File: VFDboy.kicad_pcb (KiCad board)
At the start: 2 copper layers, 139.5 x 60 mm, 120 parts, among them J1 AVR-ISP-6, J2 USB_C_Receptacle_USB2.0, J3 Micro_SD_Card_Det, J4 TagConnect_TC2030_SWD, Q1 FS8205A, Q2 S9015, Q3 AO3401A, Q4 AO3401A, Q5 S9015, Q6 2N7002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

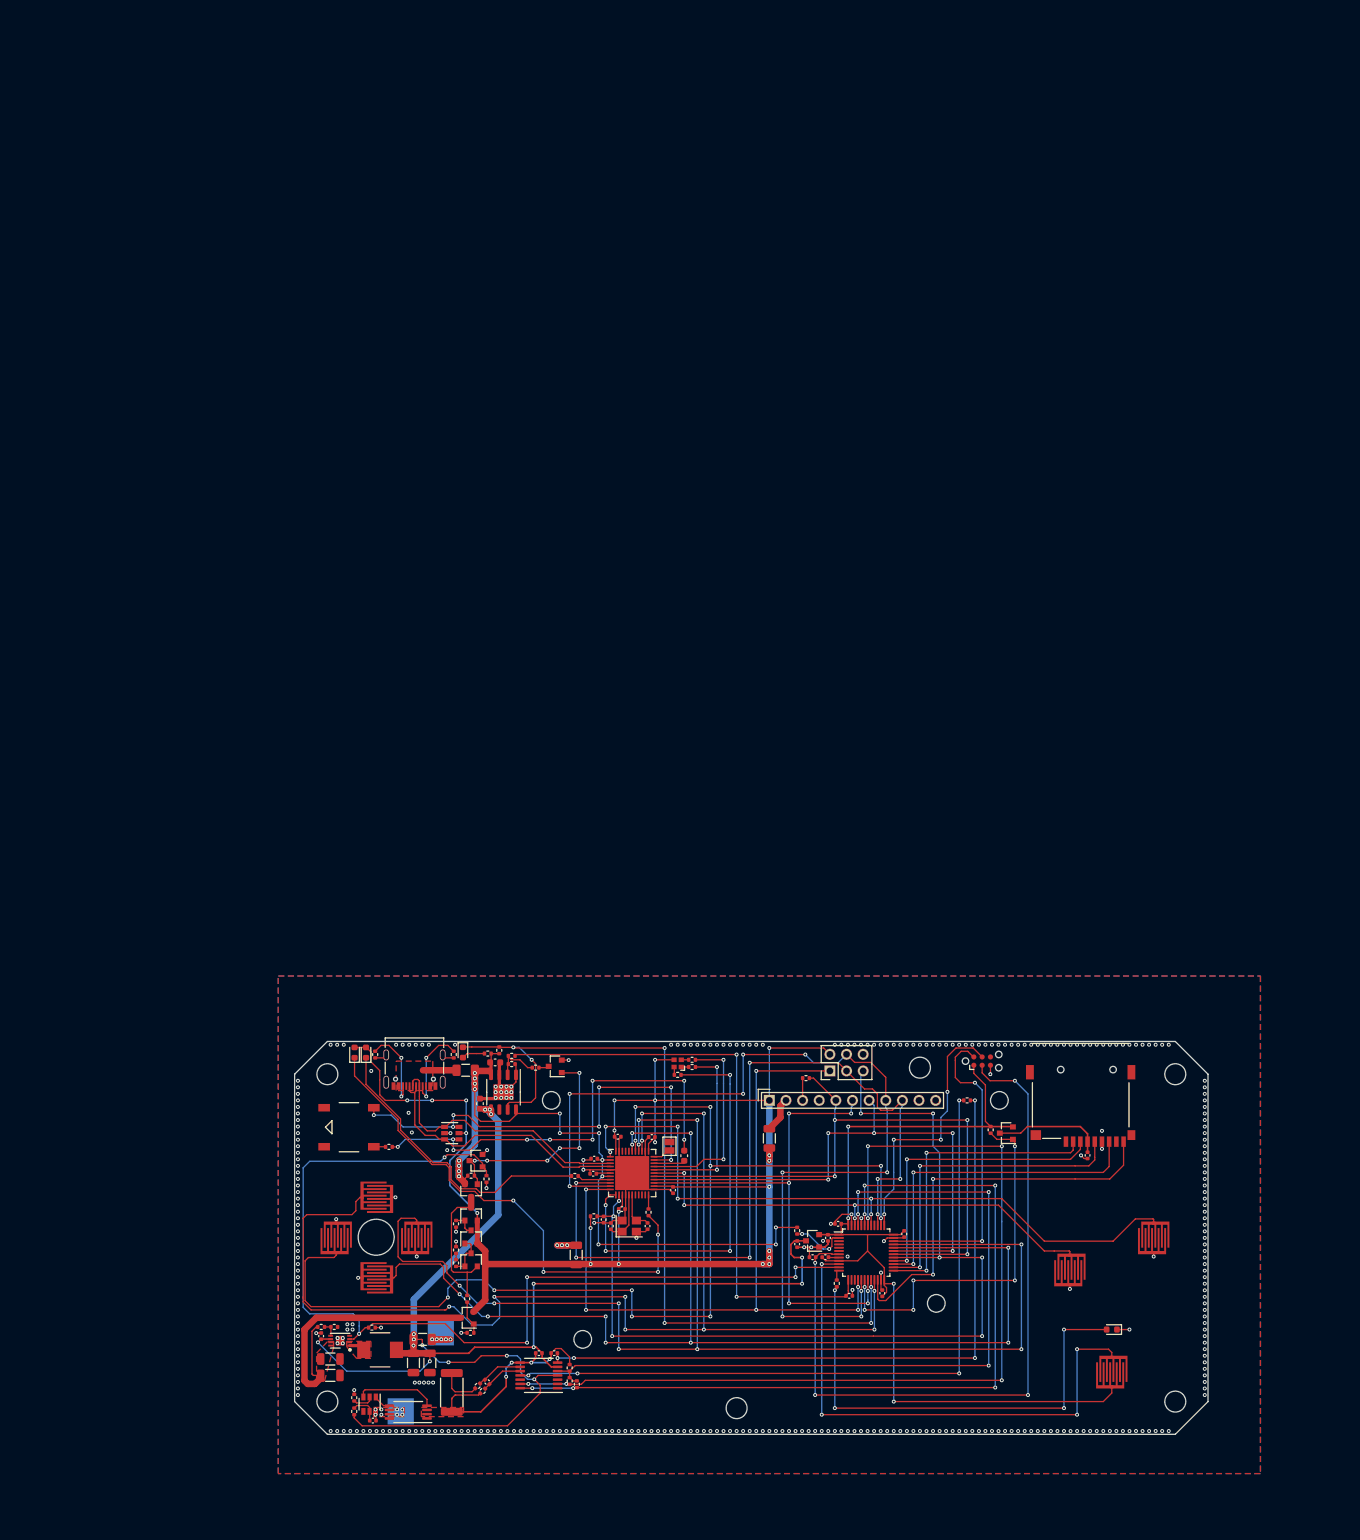
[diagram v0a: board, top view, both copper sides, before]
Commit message: Replace test points by battery footprints
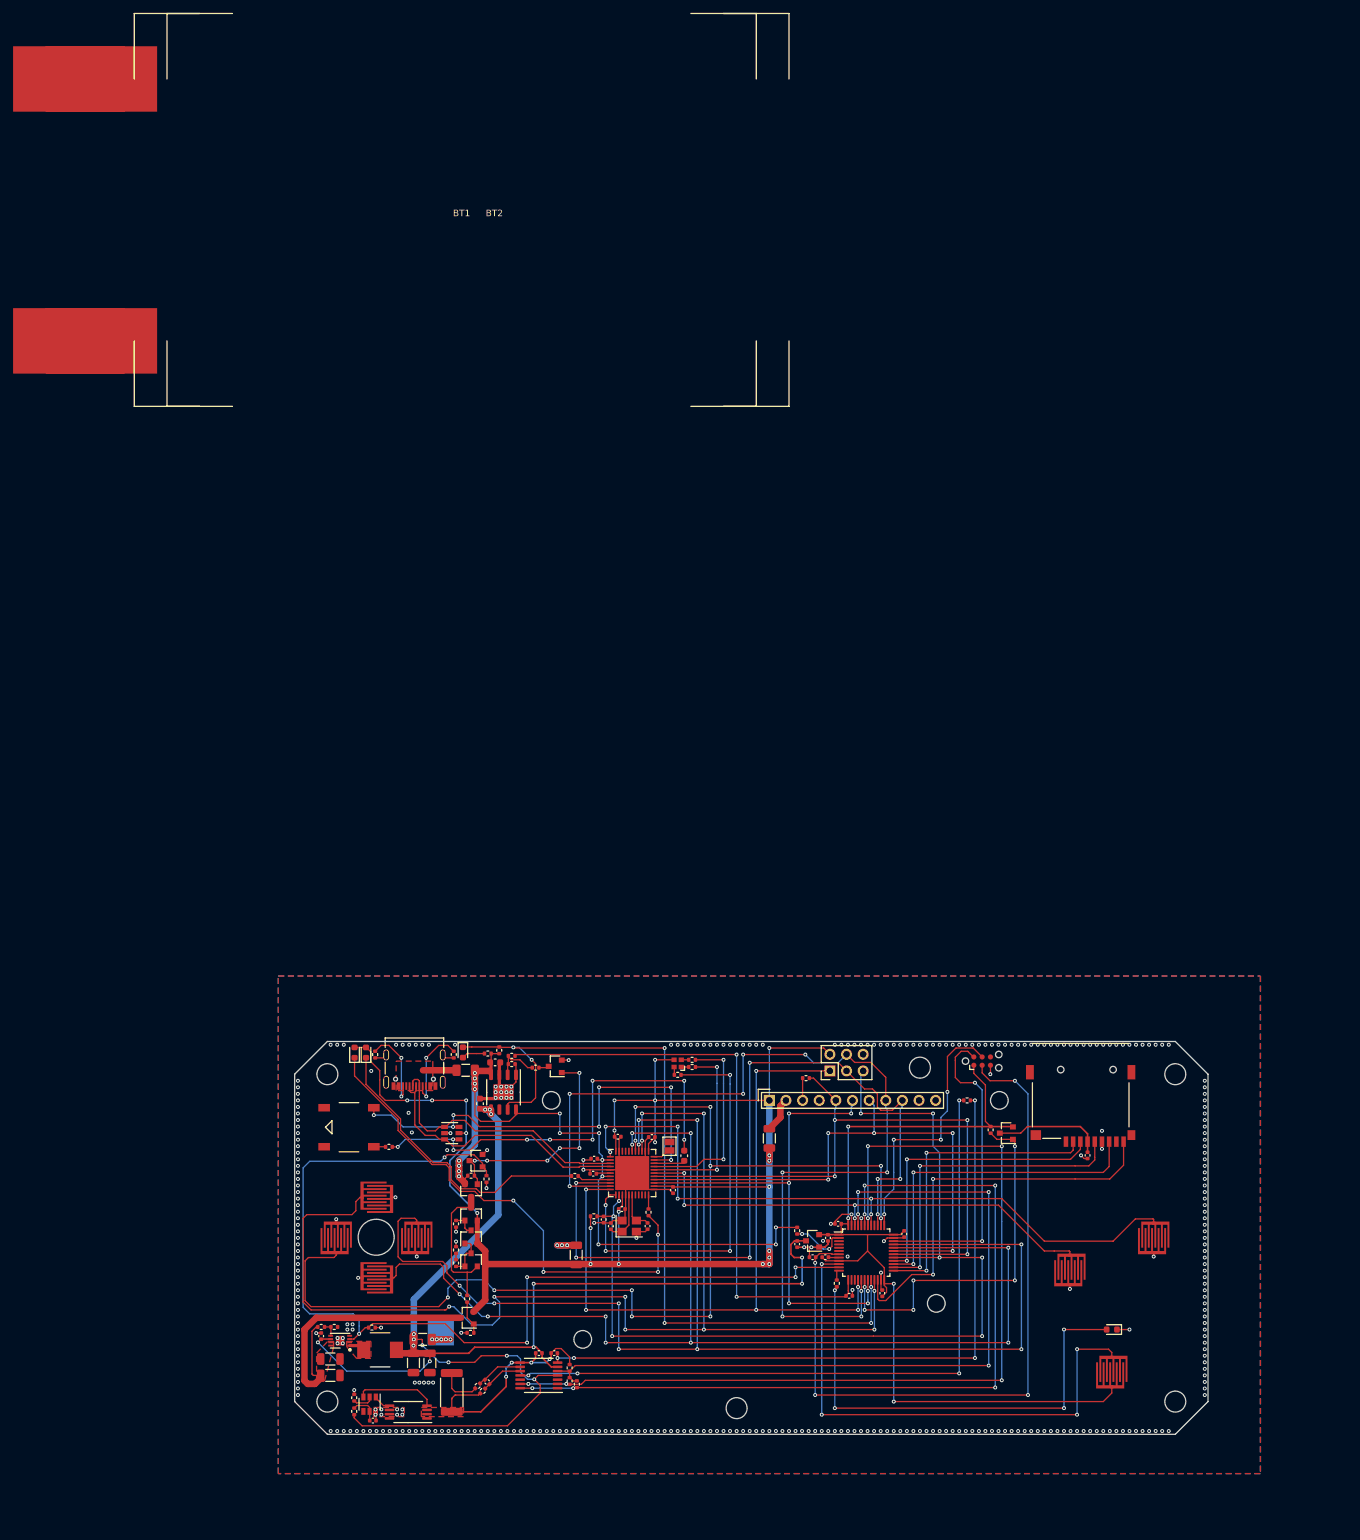
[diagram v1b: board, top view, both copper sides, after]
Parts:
- removed TP2: BAT-, TestPoint:TestPoint_Pad_4.0x4.0mm
- added BT1: 6060100, Battery_LiPo:LiPo_6060100, F.Cu at (128.0, -27.0)
- added BT2: 606090, Battery_LiPo:LiPo_606090, F.Cu at (128.0, -27.0)
- F1, F2: value Fuse -> 2A
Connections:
- F2 pad 1: +BATT -> Net-(BT1-Pad1)
- F2 pad 2: Net-(F2-Pad2) -> +BATT
- R12 pad 1: Net-(R12-Pad1) -> GND
- R12 pad 2: GND -> Net-(R12-Pad2)
- R13 pad 1: +BATT -> Net-(C18-Pad2)
- R13 pad 2: Net-(C18-Pad2) -> +BATT
- TP1 pad 1: Net-(F2-Pad2) -> Net-(TP1-Pad1)
- U5 pad 2: Net-(R12-Pad1) -> Net-(R12-Pad2)
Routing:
- net Net-(R12-Pad2): track 0.00 -> 0.69 mm, vias 0 -> 1
- net GND: track 108.1 -> 107.4 mm, vias 371 -> 370

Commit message: Route SD interface
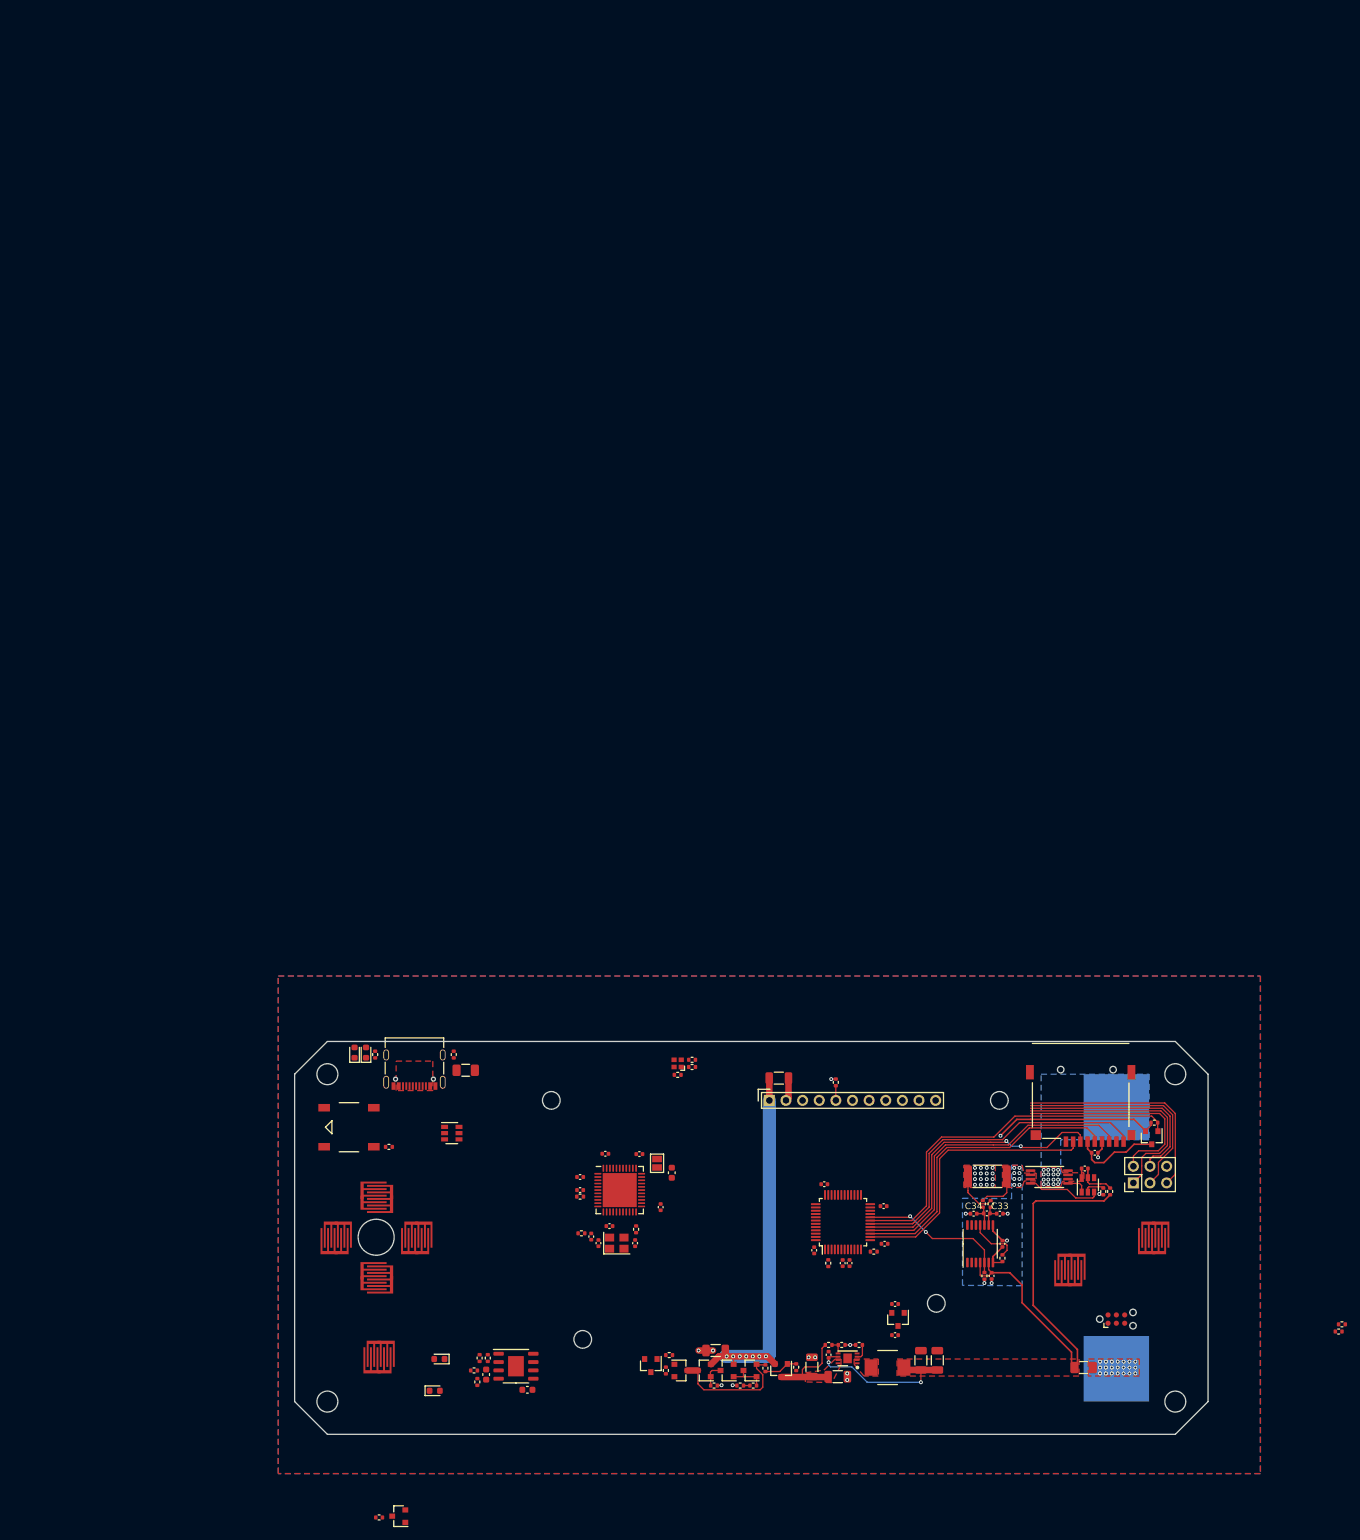
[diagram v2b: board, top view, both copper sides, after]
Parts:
- removed BT2: 606090, Battery_LiPo:LiPo_606090
- removed H4, H6: MountingHole, MountingHole:MountingHole_3.2mm_M3
- removed TP1: BAT+, TestPoint:TestPoint_Pad_4.0x4.0mm
- added C33: 100nF, Capacitor_SMD:C_0402_1005Metric, F.Cu at (210.2, 126.3)
- added C34: 100nF, Capacitor_SMD:C_0402_1005Metric, F.Cu at (206.2, 126.3)
- BT1: moved to B.Cu
- D4: value LED -> CHG
- moved BT1 162.5 mm to (170.0, 130.0), turned to 180 degrees
- moved R13 120.2 mm to (227.1, 122.9), turned to 270 degrees
- moved R12 118.7 mm to (226.0, 122.9)
- moved R34 118.3 mm to (262.4, 143.2), turned to 0 degrees
- moved R33 116.6 mm to (261.9, 144.3), turned to 0 degrees
- moved C18 115.3 mm to (223.2, 119.4), turned to 0 degrees
- moved U5 114.7 mm to (223.7, 121.9), turned to 90 degrees
- moved SW8 111.9 mm to (115.4, 148.2)
- moved Q1 104.3 mm to (217.8, 120.7), turned to 0 degrees
- moved D5 102.8 mm to (124.6, 148.5)
- moved F2 101.0 mm to (223.0, 149.8), turned to 180 degrees
- moved R32 88.2 mm to (208.3, 120.6), turned to 0 degrees
- moved R30 83.1 mm to (208.8, 124.8), turned to 270 degrees
- moved R31 81.5 mm to (207.6, 124.8), turned to 90 degrees
- moved C29 80.5 mm to (208.2, 126.3), turned to 180 degrees
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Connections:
- J3 pad 10: Net-(J3-Pad10) -> /STM32/SD_~DET
- J3 pad 2: Net-(J3-Pad2) -> /STM32/SD_~CS
- J3 pad 3: Net-(J3-Pad3) -> /STM32/SD_MOSI
- J3 pad 5: Net-(J3-Pad5) -> /STM32/SD_SCK
- J3 pad 7: Net-(J3-Pad7) -> /STM32/SD_MISO
- Q9 pad 3: Net-(C20-Pad1) -> /STM32/SD_PWR
- R12 pad 1: GND -> GNDREF
- U8 pad 14: Net-(U8-Pad14) -> /STM32/SD_~CS
- U8 pad 15: Net-(U8-Pad15) -> /STM32/SD_SCK
- U8 pad 16: /MISO -> /STM32/SD_MISO
- U8 pad 17: /MOSI -> /STM32/SD_MOSI
- U8 pad 18: Net-(Q9-Pad1) -> /STM32/SD_~DET
- U8 pad 19: /~DC -> Net-(Q9-Pad1)
- U8 pad 20: /Power/LEDchg -> /Power/GAUGE_EN
- U8 pad 22: Net-(J3-Pad10) -> /Power/LEDchg
- U8 pad 25: Net-(J3-Pad2) -> Net-(U8-Pad25)
- U8 pad 26: Net-(J3-Pad5) -> /SCK
- U8 pad 27: Net-(J3-Pad7) -> /MISO
- U8 pad 28: Net-(J3-Pad3) -> /MOSI
- U8 pad 39: /SCK -> Net-(U8-Pad39)
- U8 pad 45: /Power/GAUGE_EN -> /~DC
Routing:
- net /RIGHT: track 199.2 -> 0.00 mm, vias 10 -> 0
- net /DOWN: track 179.8 -> 0.00 mm, vias 10 -> 0
- net /UP: track 178.6 -> 0.00 mm, vias 10 -> 0
- net /LEFT: track 166.4 -> 0.00 mm, vias 11 -> 0
- net /Power/PWR_EN: track 151.8 -> 2.47 mm, vias 6 -> 0
- net +5V: track 237.9 -> 94.0 mm, vias 22 -> 7
- net /Power/SCL: track 142.2 -> 0.00 mm, vias 6 -> 0
- net /Power/SDA: track 129.4 -> 0.00 mm, vias 6 -> 0
- net /Power/LEDchg: track 126.2 -> 0.00 mm, vias 6 -> 0
- net +BATT: track 220.2 -> 95.0 mm, vias 16 -> 2
- net /MOSI: track 147.4 -> 31.4 mm, vias 10 -> 0
- net VBUS: track 115.6 -> 0.00 mm, vias 16 -> 0
- net +3V3: track 139.8 -> 25.6 mm, vias 4 -> 1
- net /STM32/~STMRST: track 112.9 -> 0.00 mm, vias 4 -> 0
- net /~RST: track 146.6 -> 33.9 mm, vias 8 -> 0
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- added copper zone on F.Cu, net +BATT
- added copper zone on B.Cu, net GNDREF
- added copper zone on F.Cu, net Net-(BT1-Pad1)
- added copper zone on B.Cu, net Net-(BT1-Pad2)

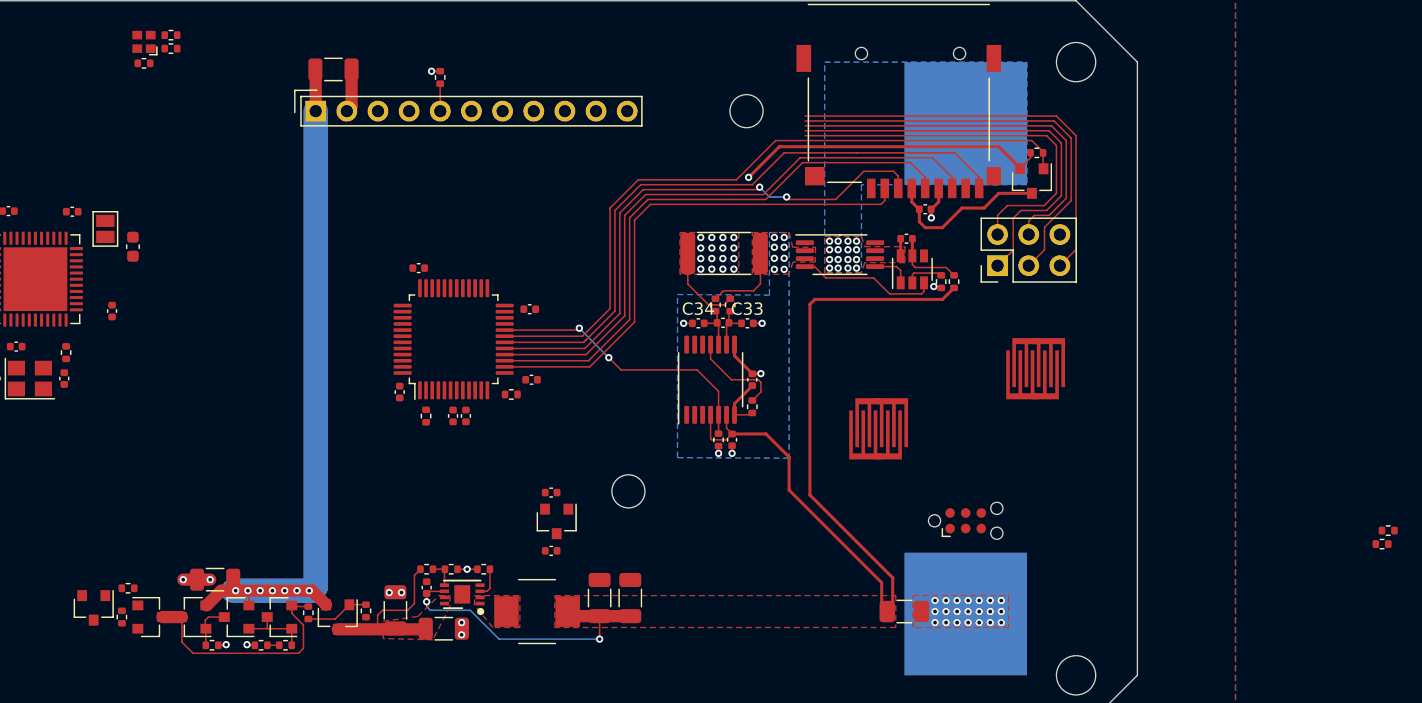
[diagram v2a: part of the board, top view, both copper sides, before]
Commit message: Hookup VFD
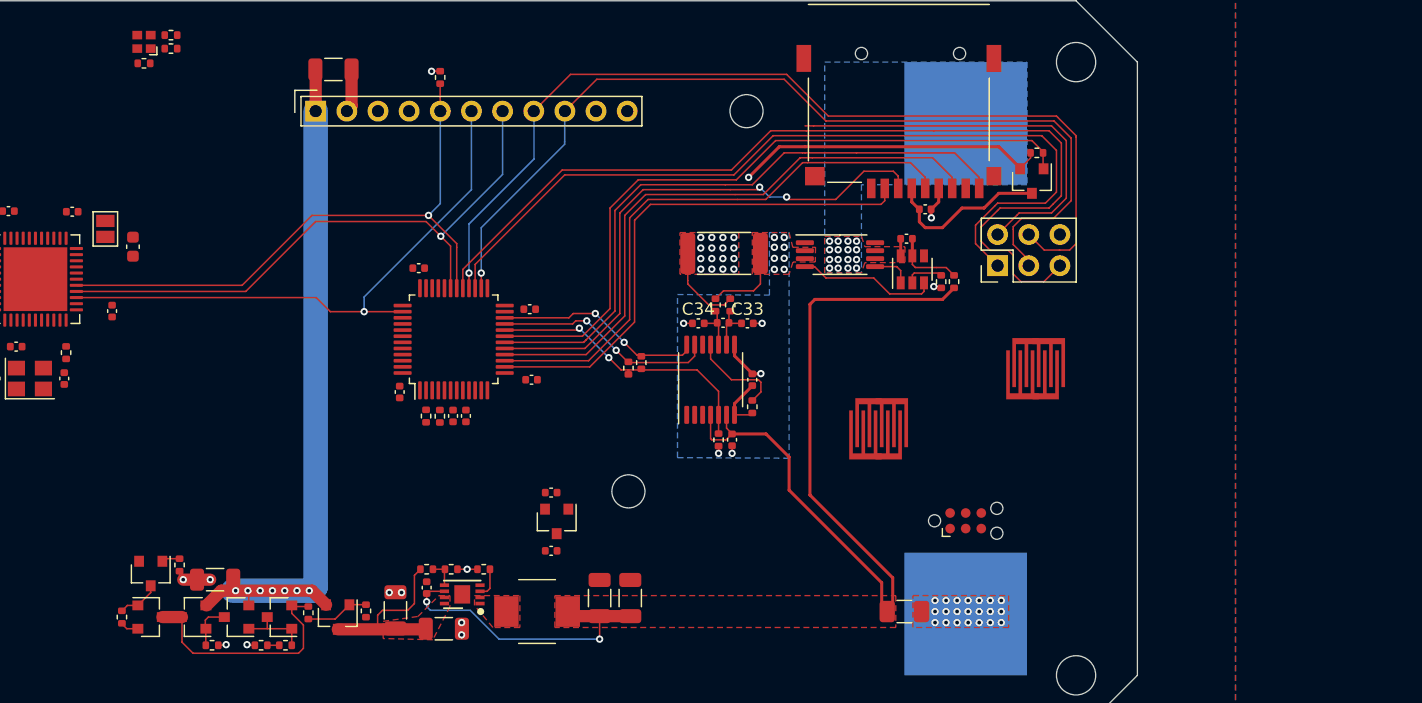
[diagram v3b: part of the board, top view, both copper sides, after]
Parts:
- moved R34 63.4 mm to (200.5, 129.9), turned to 270 degrees
- moved R33 62.2 mm to (201.6, 129.5), turned to 270 degrees
- moved R25 6.09 mm to (185.1, 133.9), turned to 90 degrees
- moved Q6 5.43 mm to (161.6, 146.7)
- moved R35 4.61 mm to (163.9, 146.0), turned to 270 degrees
- turned SW2 to 180 degrees
- turned SW6 to 180 degrees
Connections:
- R25 pad 2: Net-(R25-Pad2) -> /STM32/LED_PWR
- U8 pad 11: /Power/PWR_EN -> /Power/LEDchg
- U8 pad 12: Net-(R25-Pad2) -> /Power/PWR_EN
- U8 pad 21: /UP -> /Power/SCL
- U8 pad 22: /Power/LEDchg -> /Power/SDA
- U8 pad 3: Net-(U8-Pad3) -> /STM32/LED_PWR
- U8 pad 32: /DOWN -> Net-(U8-Pad32)
- U8 pad 33: /RIGHT -> /STM32/LED_DATA
- U8 pad 38: /LEFT -> /~DC
- U8 pad 39: Net-(U8-Pad39) -> /RIGHT
- U8 pad 41: /A -> /DOWN
- U8 pad 42: /Power/SCL -> /LEFT
- U8 pad 43: /Power/SDA -> /UP
- U8 pad 45: /~DC -> /B
- U8 pad 46: /B -> /A
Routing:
- net /~CS: track 0.00 -> 49.4 mm, vias 0 -> 1
- net /~DC: track 0.00 -> 47.1 mm, vias 0 -> 1
- net /~OLEDRST: track 2.24 -> 49.1 mm, vias 0 -> 1
- net /MOSI: track 31.4 -> 77.6 mm, vias 0 -> 1
- net /~RST: track 33.9 -> 77.7 mm
- net /SCK: track 34.1 -> 76.0 mm, vias 0 -> 1
- net /MISO: track 34.7 -> 69.3 mm
- net /Power/SCL: track 0.00 -> 18.2 mm, vias 0 -> 2
- net /Power/SDA: track 0.00 -> 17.1 mm, vias 0 -> 2
- net /Power/~PWR_EN: track 0.00 -> 3.52 mm
- net +5V: track 94.0 -> 95.5 mm
- net VBUS: track 0.00 -> 1.47 mm
- net /Power/PWR_EN: track 2.47 -> 3.87 mm
- net GND: track 19.0 -> 19.8 mm
